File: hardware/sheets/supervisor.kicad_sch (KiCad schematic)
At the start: 20 parts, among them J1 QSPI_FLASH, J2 USB_HOST, J3 POST_HEX, J4 CONSOLE, J5 SWD, U1 RP2040, Y1 12MHz

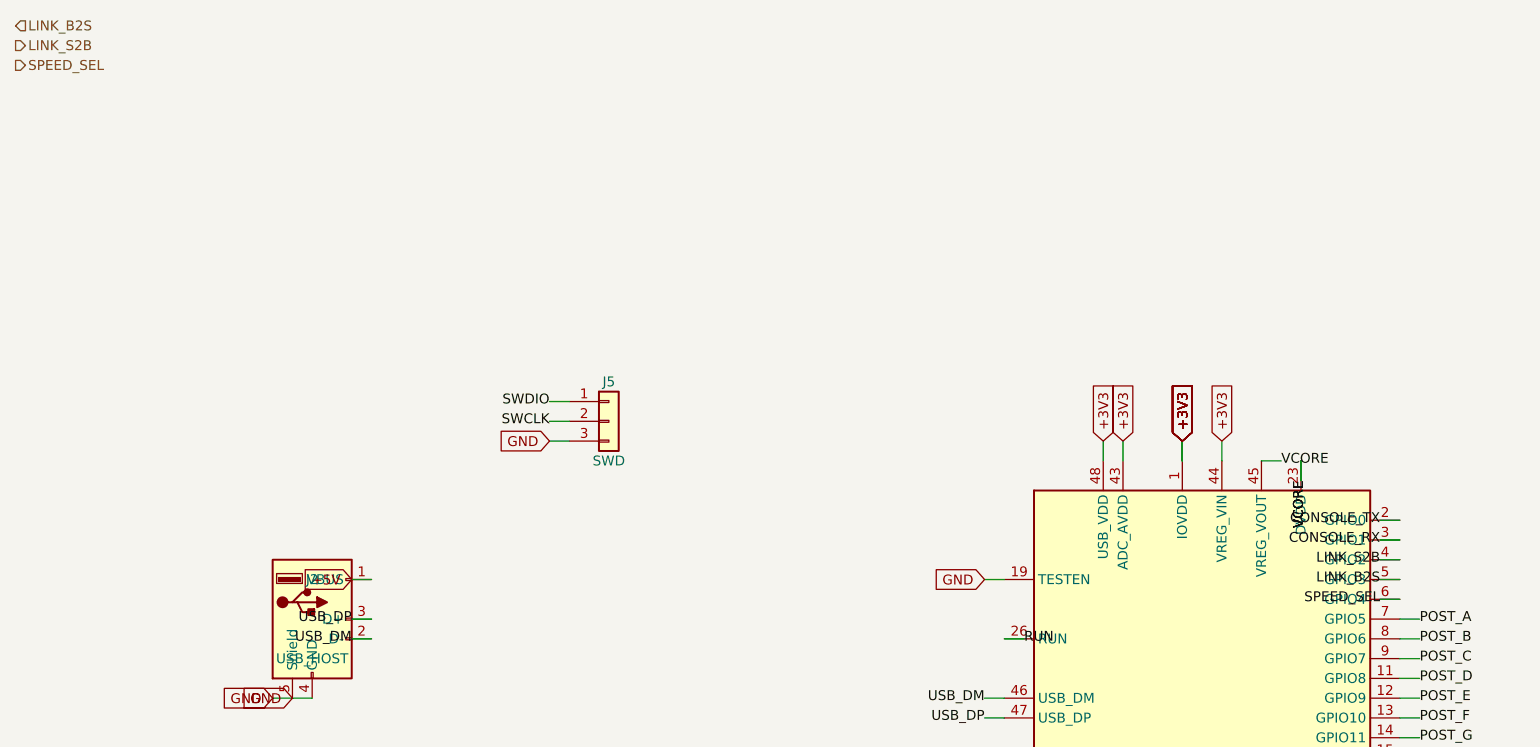
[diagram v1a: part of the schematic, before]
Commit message: Move speed-select latch from Supervisor to Bus MCU
SPEED_SEL now originates on the Bus MCU (GPIO42) and drives the cpu_core clock
mux; the Supervisor sends the divisor choice over the UART link instead, dropping
its cross-sheet interface to the 2-wire link + power. To stay within the 48-GPIO
budget, the address/control transceiver direction is now HLDA-derived externally
(per S5.2) rather than a dedicated BUSDIR GPIO. Bus MCU now owns both reset
sequencing and speed-select. Netlist verified; zero structural ERC errors.

Co-Authored-By: Claude Opus 4.8 (1M context) <noreply@anthropic.com>
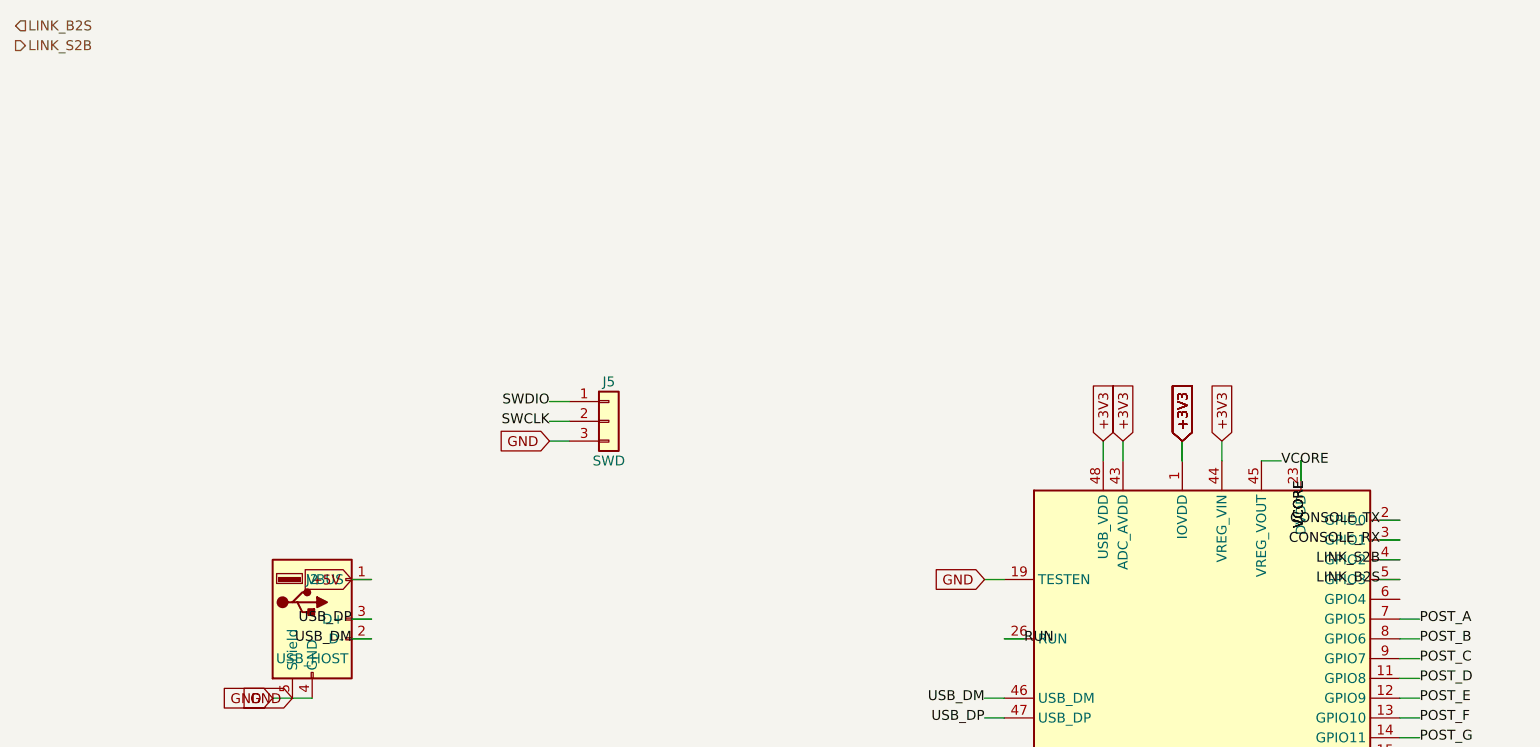
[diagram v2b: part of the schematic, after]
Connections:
- net SPEED_SEL: no longer names the net of U1.6 (GPIO4)
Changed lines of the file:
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@@
-		)
-	)
-	(hierarchical_label "SPEED_SEL"
-		(shape output)
-		(at 25.4 30.48 0)
-		(effects
-			(font
-				(size 1.27 1.27)
-			)
 		)
 	)
@@
 	(label "LINK_B2S"
 		(at 200.66 96.52 180)
-		(effects
-			(font
-				(size 1.27 1.27)
-			)
-		)
-	)
-	(wire
-		(pts
-			(xy 203.2 99.06)
-			(xy 200.66 99.06)
-		)
-		(stroke
-			(width 0)
-			(type default)
-		)
-	)
-	(label "SPEED_SEL"
-		(at 200.66 99.06 180)
 		(effects
 			(font
@@
 		(instances
 			(project "mini-xt"
-				(path "/12a90590-121b-4b08-bc73-62c223de1072/cb5ff320-ff56-4a94-bc89-c14fb0264b52"
+				(path "/e080ba29-8ec9-4601-9572-fbaf5ae0d583/afd8bf3d-a45d-42b2-8e72-5461ed0b5789"
 					(reference "U301")
 					(unit 1)
@@
 		(instances
 			(project "mini-xt"
-				(path "/12a90590-121b-4b08-bc73-62c223de1072/cb5ff320-ff56-4a94-bc89-c14fb0264b52"
+				(path "/e080ba29-8ec9-4601-9572-fbaf5ae0d583/afd8bf3d-a45d-42b2-8e72-5461ed0b5789"
 					(reference "Y301")
 					(unit 1)
@@
 		(instances
 			(project "mini-xt"
-				(path "/12a90590-121b-4b08-bc73-62c223de1072/cb5ff320-ff56-4a94-bc89-c14fb0264b52"
+				(path "/e080ba29-8ec9-4601-9572-fbaf5ae0d583/afd8bf3d-a45d-42b2-8e72-5461ed0b5789"
 					(reference "C301")
 					(unit 1)
@@
 		(instances
 			(project "mini-xt"
-				(path "/12a90590-121b-4b08-bc73-62c223de1072/cb5ff320-ff56-4a94-bc89-c14fb0264b52"
+				(path "/e080ba29-8ec9-4601-9572-fbaf5ae0d583/afd8bf3d-a45d-42b2-8e72-5461ed0b5789"
 					(reference "C302")
 					(unit 1)
@@
 		(instances
 			(project "mini-xt"
-				(path "/12a90590-121b-4b08-bc73-62c223de1072/cb5ff320-ff56-4a94-bc89-c14fb0264b52"
+				(path "/e080ba29-8ec9-4601-9572-fbaf5ae0d583/afd8bf3d-a45d-42b2-8e72-5461ed0b5789"
 					(reference "R301")
 					(unit 1)
@@
 		(instances
 			(project "mini-xt"
-				(path "/12a90590-121b-4b08-bc73-62c223de1072/cb5ff320-ff56-4a94-bc89-c14fb0264b52"
+				(path "/e080ba29-8ec9-4601-9572-fbaf5ae0d583/afd8bf3d-a45d-42b2-8e72-5461ed0b5789"
 					(reference "C303")
 					(unit 1)
@@
 		(instances
 			(project "mini-xt"
-				(path "/12a90590-121b-4b08-bc73-62c223de1072/cb5ff320-ff56-4a94-bc89-c14fb0264b52"
+				(path "/e080ba29-8ec9-4601-9572-fbaf5ae0d583/afd8bf3d-a45d-42b2-8e72-5461ed0b5789"
 					(reference "J301")
 					(unit 1)
@@
 		(instances
 			(project "mini-xt"
-				(path "/12a90590-121b-4b08-bc73-62c223de1072/cb5ff320-ff56-4a94-bc89-c14fb0264b52"
+				(path "/e080ba29-8ec9-4601-9572-fbaf5ae0d583/afd8bf3d-a45d-42b2-8e72-5461ed0b5789"
 					(reference "C304")
 					(unit 1)
@@
 		(instances
 			(project "mini-xt"
-				(path "/12a90590-121b-4b08-bc73-62c223de1072/cb5ff320-ff56-4a94-bc89-c14fb0264b52"
+				(path "/e080ba29-8ec9-4601-9572-fbaf5ae0d583/afd8bf3d-a45d-42b2-8e72-5461ed0b5789"
 					(reference "J302")
 					(unit 1)
@@
 		(instances
 			(project "mini-xt"
-				(path "/12a90590-121b-4b08-bc73-62c223de1072/cb5ff320-ff56-4a94-bc89-c14fb0264b52"
+				(path "/e080ba29-8ec9-4601-9572-fbaf5ae0d583/afd8bf3d-a45d-42b2-8e72-5461ed0b5789"
 					(reference "J303")
 					(unit 1)
@@
 		(instances
 			(project "mini-xt"
-				(path "/12a90590-121b-4b08-bc73-62c223de1072/cb5ff320-ff56-4a94-bc89-c14fb0264b52"
+				(path "/e080ba29-8ec9-4601-9572-fbaf5ae0d583/afd8bf3d-a45d-42b2-8e72-5461ed0b5789"
 					(reference "J304")
 					(unit 1)
@@
 		(instances
 			(project "mini-xt"
-				(path "/12a90590-121b-4b08-bc73-62c223de1072/cb5ff320-ff56-4a94-bc89-c14fb0264b52"
+				(path "/e080ba29-8ec9-4601-9572-fbaf5ae0d583/afd8bf3d-a45d-42b2-8e72-5461ed0b5789"
 					(reference "J305")
 					(unit 1)
@@
 		(instances
 			(project "mini-xt"
-				(path "/12a90590-121b-4b08-bc73-62c223de1072/cb5ff320-ff56-4a94-bc89-c14fb0264b52"
+				(path "/e080ba29-8ec9-4601-9572-fbaf5ae0d583/afd8bf3d-a45d-42b2-8e72-5461ed0b5789"
 					(reference "C305")
 					(unit 1)
@@
 		(instances
 			(project "mini-xt"
-				(path "/12a90590-121b-4b08-bc73-62c223de1072/cb5ff320-ff56-4a94-bc89-c14fb0264b52"
+				(path "/e080ba29-8ec9-4601-9572-fbaf5ae0d583/afd8bf3d-a45d-42b2-8e72-5461ed0b5789"
 					(reference "C306")
 					(unit 1)
@@
 		(instances
 			(project "mini-xt"
-				(path "/12a90590-121b-4b08-bc73-62c223de1072/cb5ff320-ff56-4a94-bc89-c14fb0264b52"
+				(path "/e080ba29-8ec9-4601-9572-fbaf5ae0d583/afd8bf3d-a45d-42b2-8e72-5461ed0b5789"
 					(reference "C307")
 					(unit 1)
@@
 		(instances
 			(project "mini-xt"
-				(path "/12a90590-121b-4b08-bc73-62c223de1072/cb5ff320-ff56-4a94-bc89-c14fb0264b52"
+				(path "/e080ba29-8ec9-4601-9572-fbaf5ae0d583/afd8bf3d-a45d-42b2-8e72-5461ed0b5789"
 					(reference "C308")
 					(unit 1)
@@
 		(instances
 			(project "mini-xt"
-				(path "/12a90590-121b-4b08-bc73-62c223de1072/cb5ff320-ff56-4a94-bc89-c14fb0264b52"
+				(path "/e080ba29-8ec9-4601-9572-fbaf5ae0d583/afd8bf3d-a45d-42b2-8e72-5461ed0b5789"
 					(reference "C309")
 					(unit 1)
@@
 		(instances
 			(project "mini-xt"
-				(path "/12a90590-121b-4b08-bc73-62c223de1072/cb5ff320-ff56-4a94-bc89-c14fb0264b52"
+				(path "/e080ba29-8ec9-4601-9572-fbaf5ae0d583/afd8bf3d-a45d-42b2-8e72-5461ed0b5789"
 					(reference "C310")
 					(unit 1)
@@
 		(instances
 			(project "mini-xt"
-				(path "/12a90590-121b-4b08-bc73-62c223de1072/cb5ff320-ff56-4a94-bc89-c14fb0264b52"
+				(path "/e080ba29-8ec9-4601-9572-fbaf5ae0d583/afd8bf3d-a45d-42b2-8e72-5461ed0b5789"
 					(reference "C311")
 					(unit 1)
@@
 		(instances
 			(project "mini-xt"
-				(path "/12a90590-121b-4b08-bc73-62c223de1072/cb5ff320-ff56-4a94-bc89-c14fb0264b52"
+				(path "/e080ba29-8ec9-4601-9572-fbaf5ae0d583/afd8bf3d-a45d-42b2-8e72-5461ed0b5789"
 					(reference "C312")
 					(unit 1)
